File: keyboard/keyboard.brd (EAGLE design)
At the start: 120 x 150 mm, 32 parts, among them SW1 CHERRY_MX, SW10 CHERRY_MX, SW11 CHERRY_MX, SW12 CHERRY_MX, SW13 CHERRY_MX, SW14 CHERRY_MX, SW15 CHERRY_MX, SW16 CHERRY_MX, SW17 CHERRY_MX, SW18 CHERRY_MX, SW19 CHERRY_MX, SW2 CHERRY_MX, SW20 CHERRY_MX, SW21 CHERRY_MX, SW22 CHERRY_MX, SW23 CHERRY_MX, SW24 CHERRY_MX, SW25 CHERRY_MX, SW26 CHERRY_MX, SW27 CHERRY_MX, SW28 CHERRY_MX, SW3 CHERRY_MX, SW4 CHERRY_MX, SW5 CHERRY_MX, SW6 CHERRY_MX, SW7 CHERRY_MX, SW8 CHERRY_MX, SW9 CHERRY_MX

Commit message: initial key layout
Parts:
- moved U$3 223.8 mm to (104.4, 117.3)
- moved U$5 208.8 mm to (111.0, 117.9)
- moved SW28 189.7 mm to (99.1, 16.2), turned to 340 degrees
- moved SW22 182.0 mm to (104.0, 49.4)
- moved SW26 175.7 mm to (84.5, 31.7), turned to 340 degrees
- moved SW27 170.2 mm to (78.0, 13.8), turned to 340 degrees
- moved SW20 169.0 mm to (85.0, 54.1)
- moved SW21 161.3 mm to (104.0, 68.3)
- moved SW19 159.0 mm to (66.0, 60.8)
- moved SW25 157.0 mm to (63.4, 29.2), turned to 340 degrees
- moved SW18 148.9 mm to (47.0, 65.5)
- moved SW24 137.4 mm to (9.00, 9.00)
- moved SW23 133.6 mm to (9.00, 28.0)
- moved SW17 131.5 mm to (28.0, 60.8)
- moved U$4 121.3 mm to (104.5, 110.3)
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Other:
- board size 120 x 150 mm -> 113 x 131.5 mm
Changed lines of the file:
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@@
 <setting verticaltext="up"/>
 </settings>
-<grid distance="1" unitdist="mm" unit="mm" style="lines" multiple="1" display="yes" altdistance="5" altunitdist="mil" altunit="mil"/>
+<grid distance="0.25" unitdist="mm" unit="mm" style="lines" multiple="1" display="yes" altdistance="5" altunitdist="mil" altunit="mil"/>
 <layers>
 <layer number="1" name="Top" color="4" fill="1" visible="yes" active="yes"/>
@@
 <board>
 <plain>
-<wire x1="0" y1="0" x2="120" y2="0" width="0" layer="20"/>
-<wire x1="120" y1="0" x2="120" y2="150" width="0" layer="20"/>
-<wire x1="120" y1="150" x2="0" y2="150" width="0" layer="20"/>
-<wire x1="0" y1="150" x2="0" y2="0" width="0" layer="20"/>
+<wire x1="0" y1="0" x2="113" y2="0" width="0" layer="20"/>
+<wire x1="113" y1="0" x2="113" y2="131.5" width="0" layer="20"/>
+<wire x1="113" y1="131.5" x2="0" y2="131.5" width="0" layer="20"/>
+<wire x1="0" y1="131.5" x2="0" y2="0" width="0" layer="20"/>
 </plain>
 <attributes>
@@
 </autorouter>
 <elements>
-<element name="SW1" library="cherry_mx" package="CHERRY_MX" value="CHERRY_MX" x="22.132596875" y="52.77451875"/>
-<element name="SW10" library="cherry_mx" package="CHERRY_MX" value="CHERRY_MX" x="98.132596875" y="31.87451875"/>
-<element name="SW11" library="cherry_mx" package="CHERRY_MX" value="CHERRY_MX" x="22.132596875" y="14.774515625"/>
-<element name="SW12" library="cherry_mx" package="CHERRY_MX" value="CHERRY_MX" x="41.132596875" y="19.524515625"/>
-<element name="SW13" library="cherry_mx" package="CHERRY_MX" value="CHERRY_MX" x="60.1326" y="24.27451875"/>
-<element name="SW14" library="cherry_mx" package="CHERRY_MX" value="CHERRY_MX" x="79.1326" y="19.524515625"/>
-<element name="SW15" library="cherry_mx" package="CHERRY_MX" value="CHERRY_MX" x="98.132596875" y="12.874515625"/>
-<element name="SW16" library="cherry_mx" package="CHERRY_MX" value="CHERRY_MX" x="-3.81" y="-59.24"/>
-<element name="SW17" library="cherry_mx" package="CHERRY_MX" value="CHERRY_MX" x="-3.81" y="-66.86"/>
-<element name="SW18" library="cherry_mx" package="CHERRY_MX" value="CHERRY_MX" x="-3.81" y="-74.48"/>
-<element name="SW19" library="cherry_mx" package="CHERRY_MX" value="CHERRY_MX" x="-3.81" y="-82.1"/>
-<element name="SW2" library="cherry_mx" package="CHERRY_MX" value="CHERRY_MX" x="41.132596875" y="57.524515625"/>
-<element name="SW20" library="cherry_mx" package="CHERRY_MX" value="CHERRY_MX" x="-3.81" y="-89.72"/>
-<element name="SW21" library="cherry_mx" package="CHERRY_MX" value="CHERRY_MX" x="-3.81" y="-51.62"/>
-<element name="SW22" library="cherry_mx" package="CHERRY_MX" value="CHERRY_MX" x="-3.81" y="-97.34"/>
-<element name="SW23" library="cherry_mx" package="CHERRY_MX" value="CHERRY_MX" x="-3.81" y="-104.96"/>
-<element name="SW24" library="cherry_mx" package="CHERRY_MX" value="CHERRY_MX" x="-3.81" y="-127.82"/>
-<element name="SW25" library="cherry_mx" package="CHERRY_MX" value="CHERRY_MX" x="-3.81" y="-112.58"/>
-<element name="SW26" library="cherry_mx" package="CHERRY_MX" value="CHERRY_MX" x="-3.81" y="-120.2"/>
-<element name="SW3" library="cherry_mx" package="CHERRY_MX" value="CHERRY_MX" x="60.1326" y="62.274515625"/>
-<element name="SW4" library="cherry_mx" package="CHERRY_MX" value="CHERRY_MX" x="79.1326" y="57.52451875"/>
-<element name="SW5" library="cherry_mx" package="CHERRY_MX" value="CHERRY_MX" x="98.132596875" y="50.87451875"/>
-<element name="SW6" library="cherry_mx" package="CHERRY_MX" value="CHERRY_MX" x="22.1326" y="33.774515625"/>
-<element name="SW7" library="cherry_mx" package="CHERRY_MX" value="CHERRY_MX" x="41.132596875" y="38.524515625"/>
-<element name="SW8" library="cherry_mx" package="CHERRY_MX" value="CHERRY_MX" x="60.1326" y="43.274515625"/>
-<element name="SW9" library="cherry_mx" package="CHERRY_MX" value="CHERRY_MX" x="79.1326" y="38.524515625"/>
-<element name="U$1" library="core51822b" package="CORE51822B" value="CORE51822B" x="-22.86" y="11.43"/>
-<element name="U$3" library="cree_plcc4_rgb_led" package="4-PLCC" value="CREE_PLCC4_RGB_LED" x="-119.38" y="114.3"/>
-<element name="U$4" library="yc164" package="YC164" value="YC164" x="-15.24" y="129.54"/>
-<element name="U$5" library="prog_header" package="PROG_HEADER" value="PROG_HEADER" x="-97.79" y="119.38"/>
-<element name="SW27" library="cherry_mx" package="CHERRY_MX" value="CHERRY_MX" x="-3.81" y="-135.44"/>
-<element name="SW28" library="cherry_mx" package="CHERRY_MX" value="CHERRY_MX" x="-3.81" y="-143.06"/>
+<element name="SW1" library="cherry_mx" package="CHERRY_MX" value="CHERRY_MX" x="9" y="113.000003125"/>
+<element name="SW10" library="cherry_mx" package="CHERRY_MX" value="CHERRY_MX" x="85" y="92.100003125"/>
+<element name="SW11" library="cherry_mx" package="CHERRY_MX" value="CHERRY_MX" x="9" y="75"/>
+<element name="SW12" library="cherry_mx" package="CHERRY_MX" value="CHERRY_MX" x="28" y="79.75"/>
+<element name="SW13" library="cherry_mx" package="CHERRY_MX" value="CHERRY_MX" x="47" y="84.500003125"/>
+<element name="SW14" library="cherry_mx" package="CHERRY_MX" value="CHERRY_MX" x="66" y="79.75"/>
+<element name="SW15" library="cherry_mx" package="CHERRY_MX" value="CHERRY_MX" x="85" y="73.1"/>
+<element name="SW16" library="cherry_mx" package="CHERRY_MX" value="CHERRY_MX" x="9" y="56"/>
+<element name="SW17" library="cherry_mx" package="CHERRY_MX" value="CHERRY_MX" x="28" y="60.75"/>
+<element name="SW18" library="cherry_mx" package="CHERRY_MX" value="CHERRY_MX" x="47" y="65.500003125"/>
+<element name="SW19" library="cherry_mx" package="CHERRY_MX" value="CHERRY_MX" x="66" y="60.75"/>
+<element name="SW2" library="cherry_mx" package="CHERRY_MX" value="CHERRY_MX" x="28" y="117.75"/>
+<element name="SW20" library="cherry_mx" package="CHERRY_MX" value="CHERRY_MX" x="85" y="54.1"/>
+<element name="SW21" library="cherry_mx" package="CHERRY_MX" value="CHERRY_MX" x="104" y="68.35"/>
+<element name="SW22" library="cherry_mx" package="CHERRY_MX" value="CHERRY_MX" x="104" y="49.35"/>
+<element name="SW23" library="cherry_mx" package="CHERRY_MX" value="CHERRY_MX" x="9" y="28"/>
+<element name="SW24" library="cherry_mx" package="CHERRY_MX" value="CHERRY_MX" x="9" y="9"/>
+<element name="SW25" library="cherry_mx" package="CHERRY_MX" value="CHERRY_MX" x="63.42173125" y="29.24225625" rot="R340"/>
+<element name="SW26" library="cherry_mx" package="CHERRY_MX" value="CHERRY_MX" x="84.525084375" y="31.670953125" rot="R340"/>
+<element name="SW3" library="cherry_mx" package="CHERRY_MX" value="CHERRY_MX" x="47" y="122.5"/>
+<element name="SW4" library="cherry_mx" package="CHERRY_MX" value="CHERRY_MX" x="66" y="117.750003125"/>
+<element name="SW5" library="cherry_mx" package="CHERRY_MX" value="CHERRY_MX" x="85" y="111.100003125"/>
+<element name="SW6" library="cherry_mx" package="CHERRY_MX" value="CHERRY_MX" x="9" y="94"/>
+<element name="SW7" library="cherry_mx" package="CHERRY_MX" value="CHERRY_MX" x="28" y="98.75"/>
+<element name="SW8" library="cherry_mx" package="CHERRY_MX" value="CHERRY_MX" x="47" y="103.5"/>
+<element name="SW9" library="cherry_mx" package="CHERRY_MX" value="CHERRY_MX" x="66" y="98.75"/>
+<element name="U$1" library="core51822b" package="CORE51822B" value="CORE51822B" x="36.85" y="35.18" rot="R180"/>
+<element name="U$3" library="cree_plcc4_rgb_led" package="4-PLCC" value="CREE_PLCC4_RGB_LED" x="104.37" y="117.3"/>
+<element name="U$4" library="yc164" package="YC164" value="YC164" x="104.51" y="110.29"/>
+<element name="U$5" library="prog_header" package="PROG_HEADER" value="PROG_HEADER" x="110.96" y="117.88"/>
+<element name="SW27" library="cherry_mx" package="CHERRY_MX" value="CHERRY_MX" x="78.0267" y="13.81679375" rot="R340"/>
+<element name="SW28" library="cherry_mx" package="CHERRY_MX" value="CHERRY_MX" x="99.130053125" y="16.245490625" rot="R340"/>
 </elements>
 <signals>

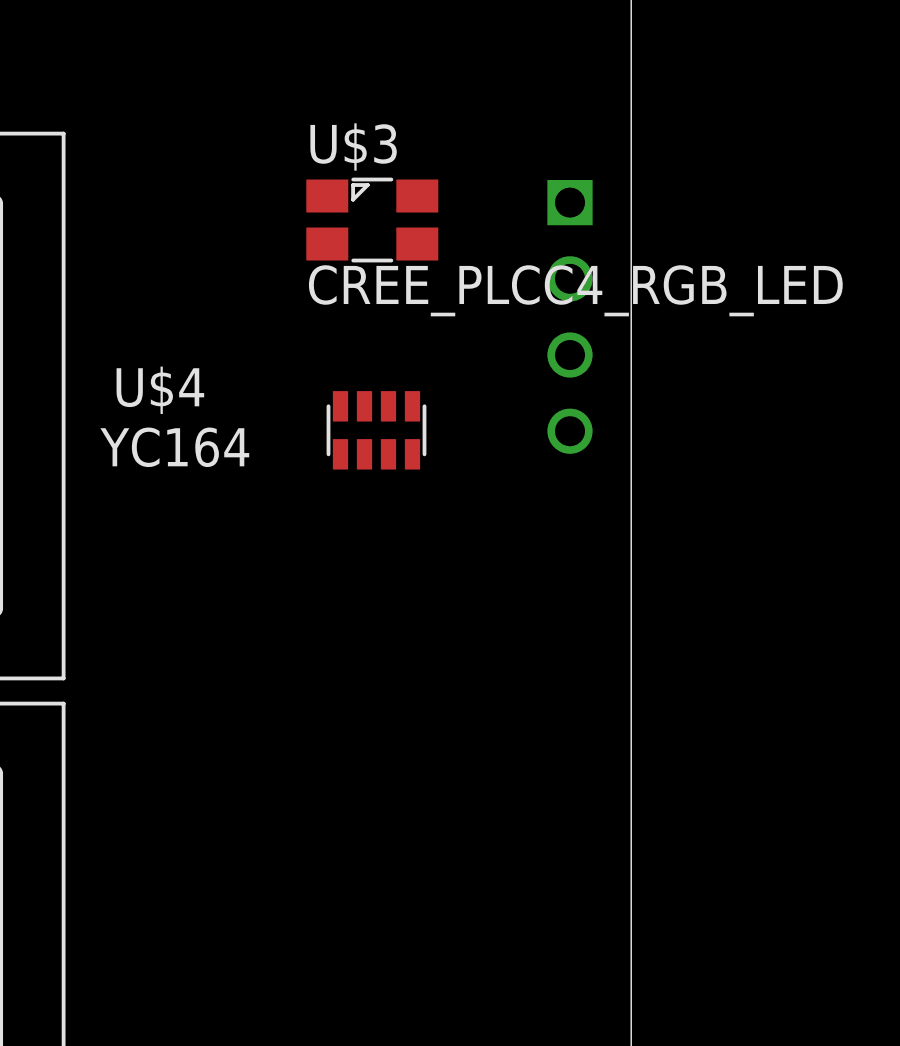
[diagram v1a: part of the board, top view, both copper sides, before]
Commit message: move header inward to allow for 90° bend
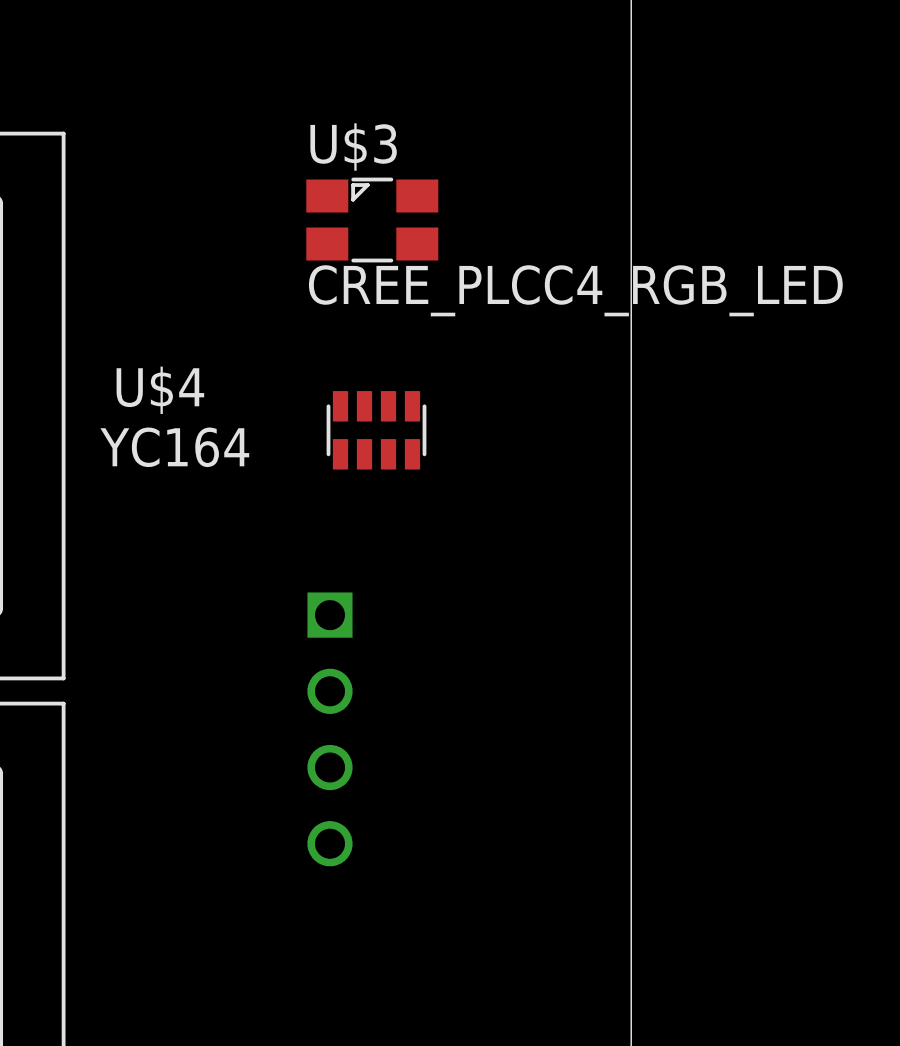
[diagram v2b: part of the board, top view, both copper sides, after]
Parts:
- moved U$5 15.9 mm to (103.0, 104.1)
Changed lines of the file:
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@@
 <element name="U$3" library="cree_plcc4_rgb_led" package="4-PLCC" value="CREE_PLCC4_RGB_LED" x="104.37" y="117.3"/>
 <element name="U$4" library="yc164" package="YC164" value="YC164" x="104.51" y="110.29"/>
-<element name="U$5" library="prog_header" package="PROG_HEADER" value="PROG_HEADER" x="110.96" y="117.88"/>
+<element name="U$5" library="prog_header" package="PROG_HEADER" value="PROG_HEADER" x="102.96" y="104.13"/>
 <element name="SW27" library="cherry_mx" package="CHERRY_MX" value="CHERRY_MX" x="78.0267" y="13.81679375" rot="R340"/>
 <element name="SW28" library="cherry_mx" package="CHERRY_MX" value="CHERRY_MX" x="99.130053125" y="16.245490625" rot="R340"/>

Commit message: wire up switches
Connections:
- new net GND: SW1.SW2A, SW1.SW2B, SW10.SW2A, SW10.SW2B, SW11.SW2A, SW11.SW2B, SW12.SW2A, SW12.SW2B, SW13.SW2A, SW13.SW2B, SW14.SW2A, SW14.SW2B, SW15.SW2A, SW15.SW2B, SW16.SW2A, SW16.SW2B, SW17.SW2A, SW17.SW2B, SW18.SW2A, SW18.SW2B, SW19.SW2A, SW19.SW2B, SW2.SW2A, SW2.SW2B, SW20.SW2A, SW20.SW2B, SW21.SW2A, SW21.SW2B, SW22.SW2A, SW22.SW2B, SW23.SW2A, SW23.SW2B, SW24.SW2A, SW24.SW2B, SW25.SW2A, SW25.SW2B, SW26.SW2A, SW26.SW2B, SW27.SW2A, SW27.SW2B, SW28.SW2A, SW28.SW2B, SW3.SW2A, SW3.SW2B, SW4.SW2A, SW4.SW2B, SW5.SW2A, SW5.SW2B, SW6.SW2A, SW6.SW2B, SW7.SW2A, SW7.SW2B, SW8.SW2A, SW8.SW2B, SW9.SW2A, SW9.SW2B, U$1.GND0, U$1.GND1
- new net SW1: SW1.SW1A, SW1.SW1B, U$1.P00
- new net SW10: SW10.SW1A, SW10.SW1B, U$1.P09
- new net SW11: SW11.SW1A, SW11.SW1B, U$1.P10
- new net SW12: SW12.SW1A, SW12.SW1B, U$1.P11
- new net SW13: SW13.SW1A, SW13.SW1B, U$1.P12
- new net SW14: SW14.SW1A, SW14.SW1B, U$1.P13
- new net SW15: SW15.SW1A, SW15.SW1B, U$1.P14
- new net SW16: SW16.SW1A, SW16.SW1B, U$1.P15
- new net SW17: SW17.SW1A, SW17.SW1B, U$1.P16
- new net SW18: SW18.SW1A, SW18.SW1B, U$1.P17
- new net SW19: SW19.SW1A, SW19.SW1B, U$1.P18
- new net SW2: SW2.SW1A, SW2.SW1B, U$1.P01
- new net SW20: SW20.SW1A, SW20.SW1B, U$1.P19
- new net SW21: SW21.SW1A, SW21.SW1B, U$1.P20
- new net SW22: SW22.SW1A, SW22.SW1B, U$1.P21
- new net SW23: SW23.SW1A, SW23.SW1B, U$1.P22
- new net SW24: SW24.SW1A, SW24.SW1B, U$1.P23
- new net SW25: SW25.SW1A, SW25.SW1B, U$1.P24
- new net SW26: SW26.SW1A, SW26.SW1B, U$1.P25
- new net SW27: SW27.SW1A, SW27.SW1B, U$1.P28
- new net SW28: SW28.SW1A, SW28.SW1B, U$1.P29
- new net SW3: SW3.SW1A, SW3.SW1B, U$1.P02
- new net SW4: SW4.SW1A, SW4.SW1B, U$1.P03
- new net SW5: SW5.SW1A, SW5.SW1B, U$1.P04
- new net SW6: SW6.SW1A, SW6.SW1B, U$1.P05
- new net SW7: SW7.SW1A, SW7.SW1B, U$1.P06
- new net SW8: SW8.SW1A, SW8.SW1B, U$1.P07
- new net SW9: SW9.SW1A, SW9.SW1B, U$1.P08
- new net SWCLK: U$1.SWCLK
- new net SWDIO: U$1.SWDIO
- new net VCC: U$1.VCC

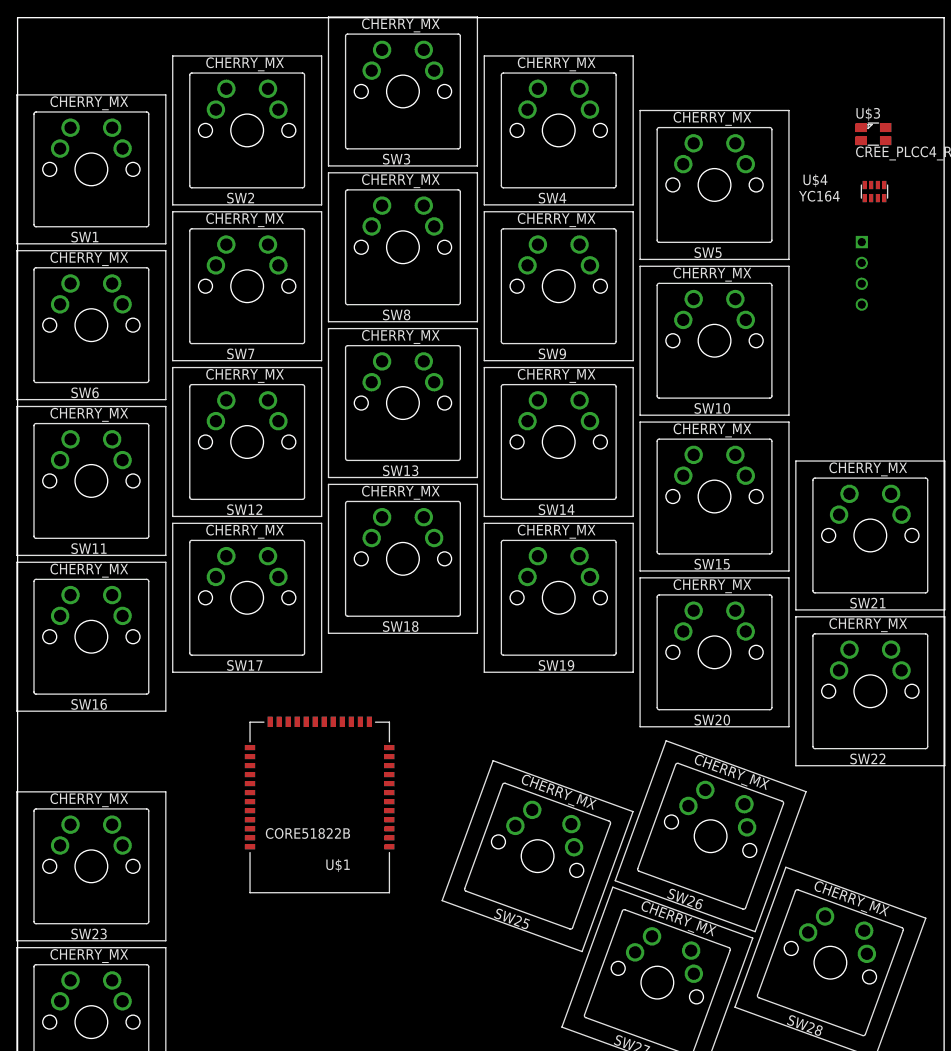
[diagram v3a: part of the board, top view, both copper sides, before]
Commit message: run autorouter
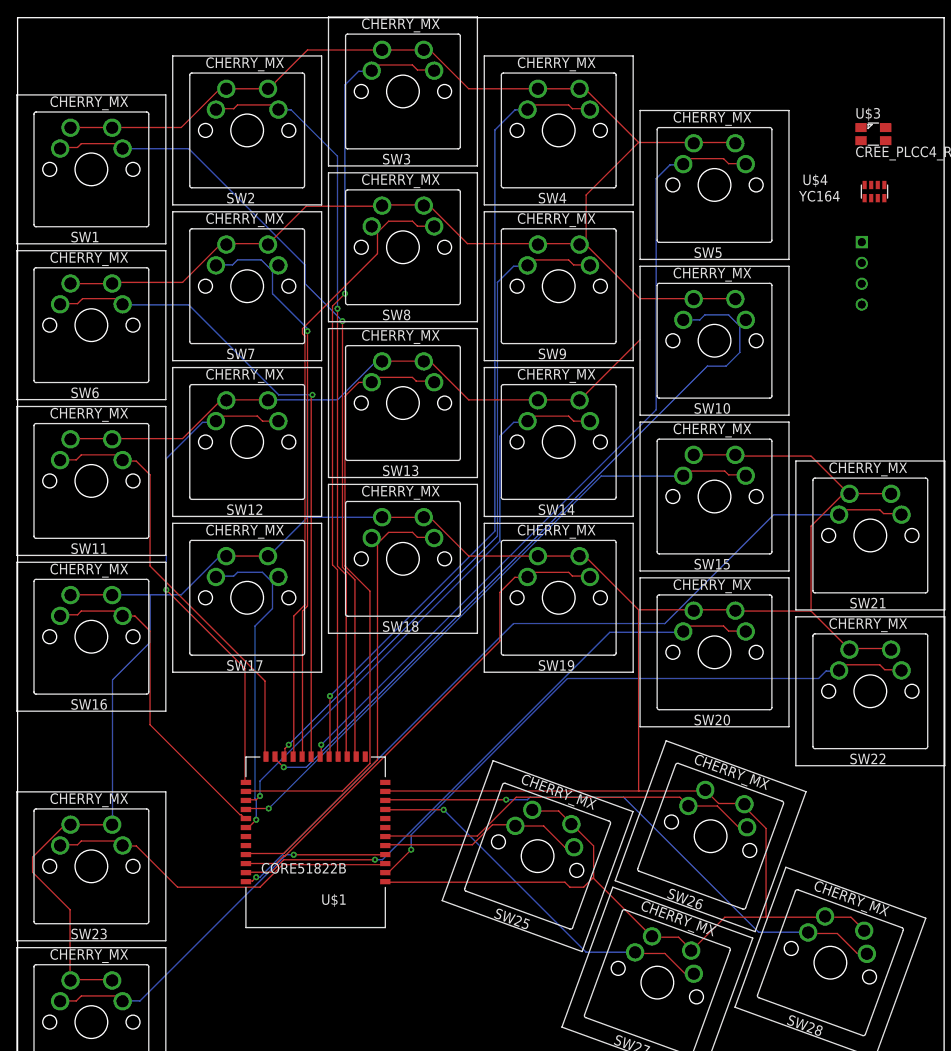
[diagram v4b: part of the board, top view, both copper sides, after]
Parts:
- moved U$1 4.28 mm to (36.4, 30.9)
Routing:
- net GND: track 0.00 -> 672.0 mm
- net SW5: track 0.00 -> 99.7 mm, vias 0 -> 1
- net SW21: track 0.00 -> 99.0 mm, vias 0 -> 1
- net SW1: track 0.00 -> 98.9 mm, vias 0 -> 1
- net SW4: track 0.00 -> 98.0 mm, vias 0 -> 1
- net SW3: track 0.00 -> 95.0 mm, vias 0 -> 1
- net SW2: track 0.00 -> 91.4 mm, vias 0 -> 1
- net SW10: track 0.00 -> 91.4 mm, vias 0 -> 1
- net SW9: track 0.00 -> 81.4 mm, vias 0 -> 1
- net SW6: track 0.00 -> 80.1 mm, vias 0 -> 1
- net SW15: track 0.00 -> 78.3 mm, vias 0 -> 1
- net SW8: track 0.00 -> 78.2 mm
- net SW22: track 0.00 -> 74.8 mm, vias 0 -> 1
- net SW13: track 0.00 -> 74.7 mm
- net SW20: track 0.00 -> 73.7 mm, vias 0 -> 1
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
